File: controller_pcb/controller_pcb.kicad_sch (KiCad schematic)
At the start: 23 parts, among them IC1 AMS1117-5.0, J1 A_08-LC-TT, J2 SM04B-GHS-TB_LF__SN_, Q1 SI2301CDS-T1-GE3.

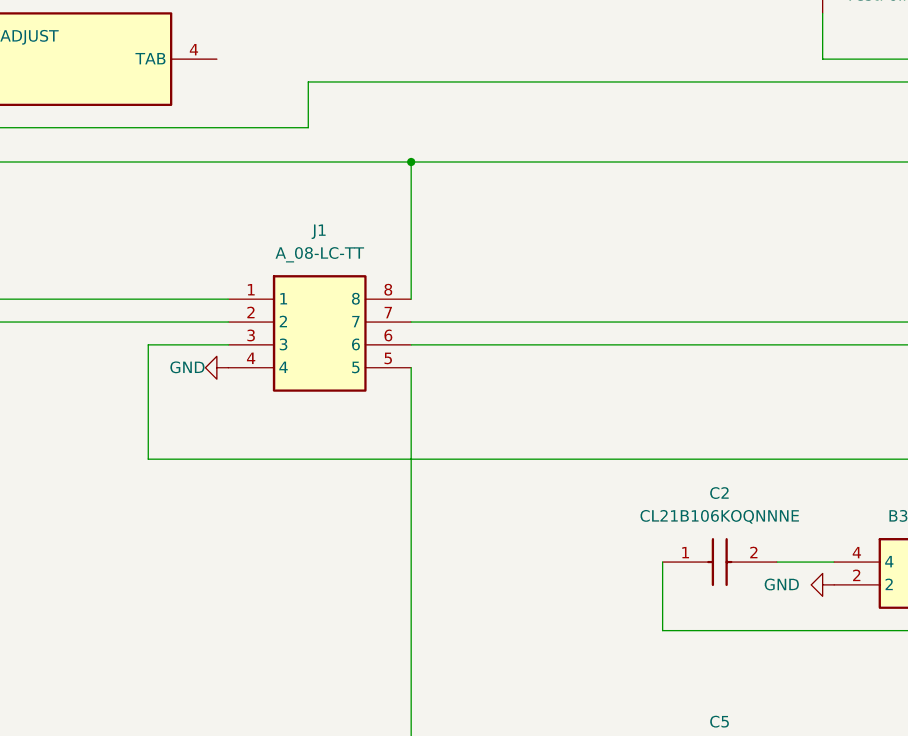
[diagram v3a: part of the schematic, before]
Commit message: added decoupling caps, modified silkscreen and some corners on routing
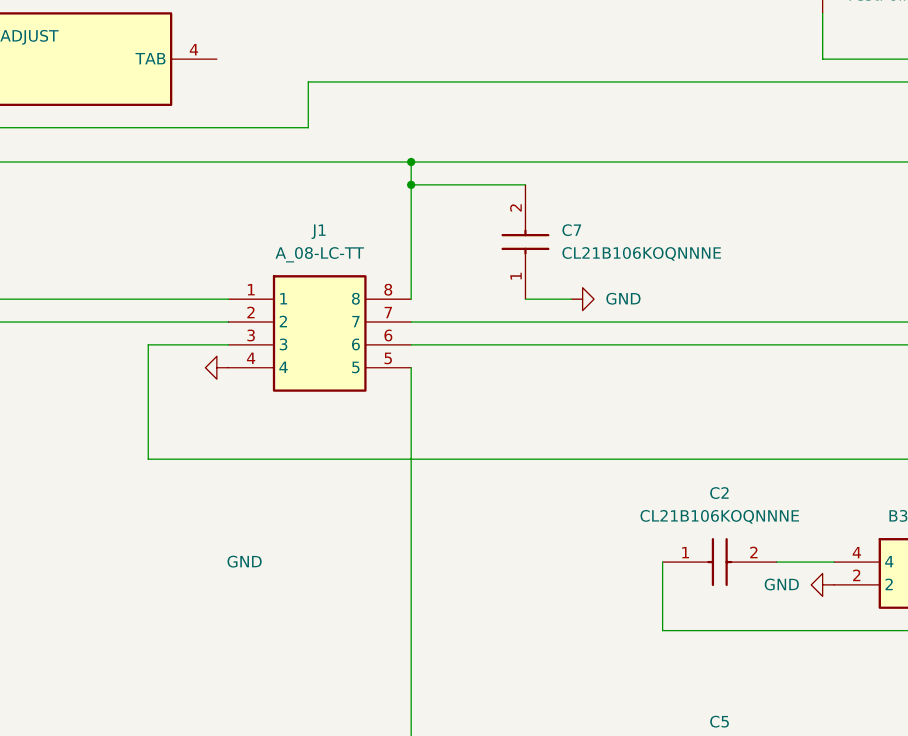
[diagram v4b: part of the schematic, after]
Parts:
- added C7: CL21B106KOQNNNE, CAPC2012X140N, symbol Controller_Comp:CL21B106KOQNNNE
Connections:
- net GND: now also C7.1
- net at IC1.2 (VOUT), J1.8, R1.2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: now also C7.2
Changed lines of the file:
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@@
 	)
 	(junction
+		(at 158.75 41.91)
+		(diameter 0)
+		(color 0 0 0 0)
+	)
+	(junction
 		(at 59.69 39.37)
 		(diameter 0)
@@
 	(wire
 		(pts
+			(xy 158.75 41.91) (xy 158.75 39.37)
+		)
+		(stroke
+			(width 0)
+			(type default)
+		)
+	)
+	(wire
+		(pts
 			(xy 232.41 81.28) (xy 232.41 59.69)
 		)
@@
 	(wire
 		(pts
-			(xy 158.75 54.61) (xy 158.75 39.37)
+			(xy 158.75 54.61) (xy 158.75 41.91)
 		)
 		(stroke
@@
 	(wire
 		(pts
+			(xy 171.45 54.61) (xy 176.53 54.61)
+		)
+		(stroke
+			(width 0)
+			(type default)
+		)
+	)
+	(wire
+		(pts
 			(xy 53.34 104.14) (xy 67.31 104.14)
 		)
@@
 	(wire
 		(pts
+			(xy 158.75 41.91) (xy 171.45 41.91)
+		)
+		(stroke
+			(width 0)
+			(type default)
+		)
+	)
+	(wire
+		(pts
 			(xy 200.66 154.94) (xy 213.36 154.94)
 		)
@@
 	)
 	(symbol
+		(lib_id "Controller_Comp:CL21B106KOQNNNE")
+		(at 171.45 54.61 90)
+		(unit 1)
+		(exclude_from_sim no)
+		(in_bom yes)
+		(on_board yes)
+		(dnp no)
+		(property "Reference" "C7"
+			(at 175.4596 46.9899 90)
+			(effects
+				(font
+					(size 1.27 1.27)
+				)
+				(justify right)
+			)
+		)
+		(property "Value" "CL21B106KOQNNNE"
+			(at 175.4596 49.5299 90)
+			(effects
+				(font
+					(size 1.27 1.27)
+				)
+				(justify right)
+			)
+		)
+		(property "Footprint" "CAPC2012X140N"
+			(at 267.64 45.72 0)
+			(effects
+				(font
+					(size 1.27 1.27)
+				)
+				(justify left top)
+				(hide yes)
+			)
+		)
+		(property "Datasheet" "https://datasheet.datasheetarchive.com/originals/distributors/Datasheets_SAMA/a6a503886ec2e900bbf4e5d6e2f8e8b0.pdf"
+			(at 367.64 45.72 0)
+			(effects
+				(font
+					(size 1.27 1.27)
+				)
+				(justify left top)
+				(hide yes)
+			)
+		)
+		(property "Description" "CAP, 10uF, 16V, +/-10%, X7R, 0805"
+			(at 176.022 47.498 0)
+			(effects
+				(font
+					(size 1.27 1.27)
+				)
+				(hide yes)
+			)
+		)
+		(property "Height" "1.4"
+			(at 567.64 45.72 0)
+			(effects
+				(font
+					(size 1.27 1.27)
+				)
+				(justify left top)
+				(hide yes)
+			)
+		)
+		(property "Manufacturer_Name" "SAMSUNG"
+			(at 667.64 45.72 0)
+			(effects
+				(font
+					(size 1.27 1.27)
+				)
+				(justify left top)
+				(hide yes)
+			)
+		)
+		(property "Manufacturer_Part_Number" "CL21B106KOQNNNE"
+			(at 767.64 45.72 0)
+			(effects
+				(font
+					(size 1.27 1.27)
+				)
+				(justify left top)
+				(hide yes)
+			)
+		)
+		(property "Mouser Part Number" "187-CL21B106KOQNNNE"
+			(at 867.64 45.72 0)
+			(effects
+				(font
+					(size 1.27 1.27)
+				)
+				(justify left top)
+				(hide yes)
+			)
+		)
+		(property "Mouser Price/Stock" "https://www.mouser.co.uk/ProductDetail/Samsung-Electro-Mechanics/CL21B106KOQNNNE?qs=349EhDEZ59r8qgLddyW2Yw%3D%3D"
+			(at 967.64 45.72 0)
+			(effects
+				(font
+					(size 1.27 1.27)
+				)
+				(justify left top)
+				(hide yes)
+			)
+		)
+		(property "Arrow Part Number" "CL21B106KOQNNNE"
+			(at 1067.64 45.72 0)
+			(effects
+				(font
+					(size 1.27 1.27)
+				)
+				(justify left top)
+				(hide yes)
+			)
+		)
+		(property "Arrow Price/Stock" "https://www.arrow.com/en/products/cl21b106koqnnne/samsung-electro-mechanics?utm_currency=USD&region=europe"
+			(at 1167.64 45.72 0)
+			(effects
+				(font
+					(size 1.27 1.27)
+				)
+				(justify left top)
+				(hide yes)
+			)
+		)
+		(pin "1"
+		)
+		(pin "2"
+		)
+		(instances
+			(project "controller_pcb"
+				(path "/35628871-c2d7-47c8-b610-2ce05008c7f9"
+					(reference "C7")
+					(unit 1)
+				)
+			)
+		)
+	)
+	(symbol
 		(lib_id "Controller_Comp:ERJP06F1002V")
 		(at 77.47 62.23 0)
@@
 		)
 		(property "Value" "GND"
-			(at 135.89 62.23 90)
+			(at 142.24 83.82 90)
 			(effects
 				(font
@@
 					(unit 1)
 				)
+			)
+		)
+	)
+	(symbol
+		(lib_id "power:GND")
+		(at 176.53 54.61 90)
+		(unit 1)
+		(exclude_from_sim no)
+		(in_bom yes)
+		(on_board yes)
+		(dnp no)
+		(fields_autoplaced yes)
+		(property "Reference" "#PWR012"
+			(at 182.88 54.61 0)
+			(effects
+				(font
+					(size 1.27 1.27)
+				)
+				(hide yes)
+			)
+		)
+		(property "Value" "GND"
+			(at 180.34 54.6099 90)
+			(effects
+				(font
+					(size 1.27 1.27)
+				)
+				(justify right)
+			)
+		)
+		(property "Footprint" ""
+			(at 176.53 54.61 0)
+			(effects
+				(font
+					(size 1.27 1.27)
+				)
+				(hide yes)
+			)
+		)
+		(property "Datasheet" ""
+			(at 176.53 54.61 0)
+			(effects
+				(font
+					(size 1.27 1.27)
+				)
+				(hide yes)
+			)
+		)
+		(property "Description" "Power symbol creates a global label with name \"GND\" , ground"
+			(at 176.53 54.61 0)
+			(effects
+				(font
+					(size 1.27 1.27)
+				)
+				(hide yes)
+			)
+		)
+		(pin "1"
+		)
+		(instances
+			(project ""
+				(path "/35628871-c2d7-47c8-b610-2ce05008c7f9"
+					(reference "#PWR012")
+					(unit 1)
+				)

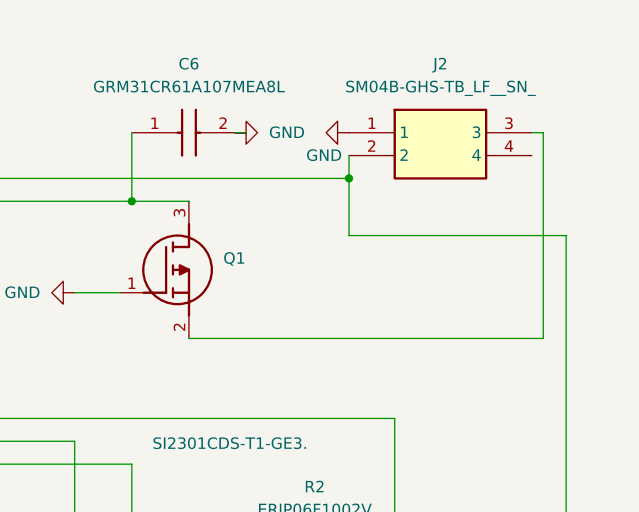
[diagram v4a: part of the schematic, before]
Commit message: added hirose DF13 to check footprints
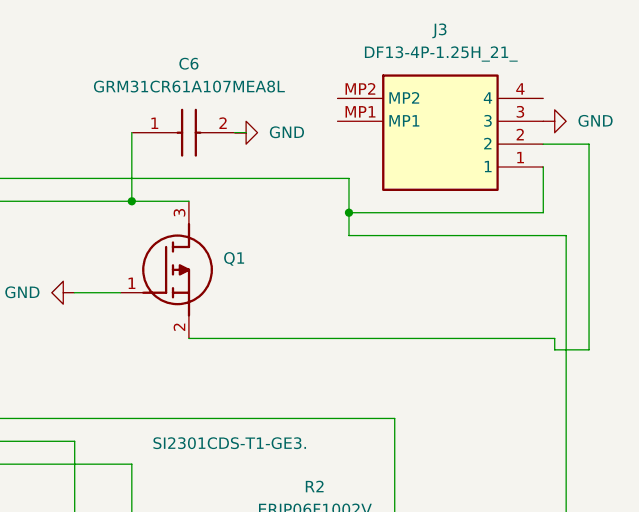
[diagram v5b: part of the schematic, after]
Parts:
- removed J2: SM04B-GHS-TB_LF__SN_, SM04B-GHS-TB, symbol Controller_Comp:SM04B-GHS-TB_LF__SN_
- added J3: DF13-4P-1.25H_21_, Controller_Footprints:DF134P125H21, symbol Controller_Comp:DF13-4P-1.25H_21_
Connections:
- net GND: now also J3.3
- net at J1.3, TP1.1: now also J3.1
- net at Q1.2 (S): now also J3.2

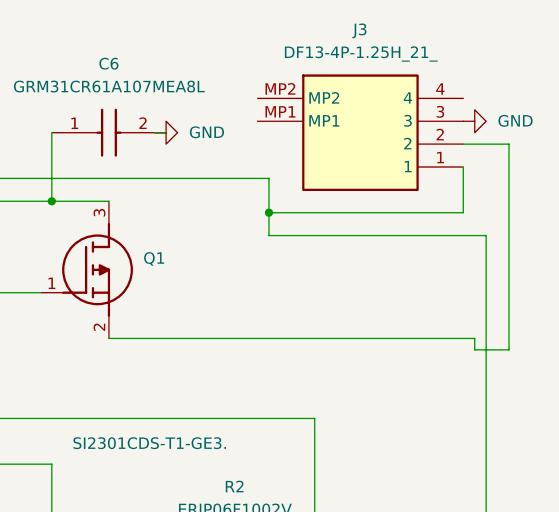
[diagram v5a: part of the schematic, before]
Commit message: updated wiring and copper fill
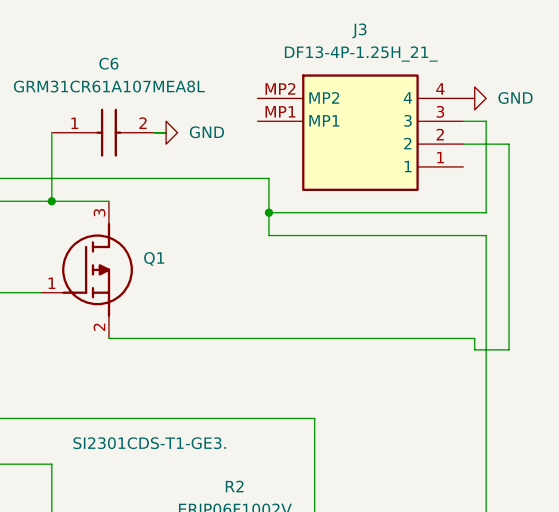
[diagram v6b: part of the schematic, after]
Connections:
- net GND: now also J3.4; no longer J3.3
- net at J1.3, TP1.1: now also J3.3; no longer J3.1
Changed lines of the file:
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@@
-	(wire
-		(pts
-			(xy 283.21 24.13) (xy 283.21 46.99)
-		)
-		(stroke
-			(width 0)
-			(type default)
-		)
-	)
 	(wire
 		(pts
@@
 	(wire
 		(pts
+			(xy 280.67 31.75) (xy 280.67 21.59)
+		)
+		(stroke
+			(width 0)
+			(type default)
+		)
+	)
+	(wire
+		(pts
 			(xy 87.63 50.8) (xy 87.63 54.61)
 		)
@@
 	(wire
 		(pts
-			(xy 283.21 24.13) (xy 278.13 24.13)
-		)
-		(stroke
-			(width 0)
-			(type default)
-		)
-	)
-	(wire
-		(pts
 			(xy 39.37 31.75) (xy 41.91 31.75)
 		)
@@
 	(wire
 		(pts
-			(xy 256.54 31.75) (xy 278.13 31.75)
+			(xy 256.54 31.75) (xy 280.67 31.75)
 		)
 		(stroke
@@
 	(wire
 		(pts
+			(xy 278.13 21.59) (xy 280.67 21.59)
+		)
+		(stroke
+			(width 0)
+			(type default)
+		)
+	)
+	(wire
+		(pts
 			(xy 59.69 39.37) (xy 158.75 39.37)
 		)
@@
 	(wire
 		(pts
-			(xy 278.13 31.75) (xy 278.13 26.67)
-		)
-		(stroke
-			(width 0)
-			(type default)
-		)
-	)
-	(wire
-		(pts
 			(xy 231.14 40.64) (xy 226.06 40.64)
 		)
@@
 	(wire
 		(pts
+			(xy 278.13 24.13) (xy 283.21 24.13)
+		)
+		(stroke
+			(width 0)
+			(type default)
+		)
+	)
+	(wire
+		(pts
 			(xy 171.45 54.61) (xy 176.53 54.61)
 		)
@@
 		(pts
 			(xy 233.68 154.94) (xy 233.68 134.62)
+		)
+		(stroke
+			(width 0)
+			(type default)
+		)
+	)
+	(wire
+		(pts
+			(xy 283.21 46.99) (xy 283.21 24.13)
 		)
 		(stroke
@@
 				(path "/35628871-c2d7-47c8-b610-2ce05008c7f9"
 					(reference "C7")
-					(unit 1)
-				)
-			)
-		)
-	)
-	(symbol
-		(lib_id "power:GND")
-		(at 278.13 21.59 90)
-		(unit 1)
-		(exclude_from_sim no)
-		(in_bom yes)
-		(on_board yes)
-		(dnp no)
-		(fields_autoplaced yes)
-		(property "Reference" "#PWR011"
-			(at 284.48 21.59 0)
-			(effects
-				(font
-					(size 1.27 1.27)
-				)
-				(hide yes)
-			)
-		)
-		(property "Value" "GND"
-			(at 281.94 21.5899 90)
-			(effects
-				(font
-					(size 1.27 1.27)
-				)
-				(justify right)
-			)
-		)
-		(property "Footprint" ""
-			(at 278.13 21.59 0)
-			(effects
-				(font
-					(size 1.27 1.27)
-				)
-				(hide yes)
-			)
-		)
-		(property "Datasheet" ""
-			(at 278.13 21.59 0)
-			(effects
-				(font
-					(size 1.27 1.27)
-				)
-				(hide yes)
-			)
-		)
-		(property "Description" "Power symbol creates a global label with name \"GND\" , ground"
-			(at 278.13 21.59 0)
-			(effects
-				(font
-					(size 1.27 1.27)
-				)
-				(hide yes)
-			)
-		)
-		(pin "1"
-		)
-		(instances
-			(project ""
-				(path "/35628871-c2d7-47c8-b610-2ce05008c7f9"
-					(reference "#PWR011")
 					(unit 1)
 				)
@@
 					(unit 1)
 				)
+			)
+		)
+	)
+	(symbol
+		(lib_id "power:GND")
+		(at 278.13 19.05 90)
+		(unit 1)
+		(exclude_from_sim no)
+		(in_bom yes)
+		(on_board yes)
+		(dnp no)
+		(fields_autoplaced yes)
+		(property "Reference" "#PWR011"
+			(at 284.48 19.05 0)
+			(effects
+				(font
+					(size 1.27 1.27)
+				)
+				(hide yes)
+			)
+		)
+		(property "Value" "GND"
+			(at 281.94 19.0499 90)
+			(effects
+				(font
+					(size 1.27 1.27)
+				)
+				(justify right)
+			)
+		)
+		(property "Footprint" ""
+			(at 278.13 19.05 0)
+			(effects
+				(font
+					(size 1.27 1.27)
+				)
+				(hide yes)
+			)
+		)
+		(property "Datasheet" ""
+			(at 278.13 19.05 0)
+			(effects
+				(font
+					(size 1.27 1.27)
+				)
+				(hide yes)
+			)
+		)
+		(property "Description" "Power symbol creates a global label with name \"GND\" , ground"
+			(at 278.13 19.05 0)
+			(effects
+				(font
+					(size 1.27 1.27)
+				)
+				(hide yes)
+			)
+		)
+		(pin "1"
+		)
+		(instances
+			(project ""
+				(path "/35628871-c2d7-47c8-b610-2ce05008c7f9"
+					(reference "#PWR011")
+					(unit 1)
+				)
